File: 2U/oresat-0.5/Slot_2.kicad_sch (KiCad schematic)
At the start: 3 parts

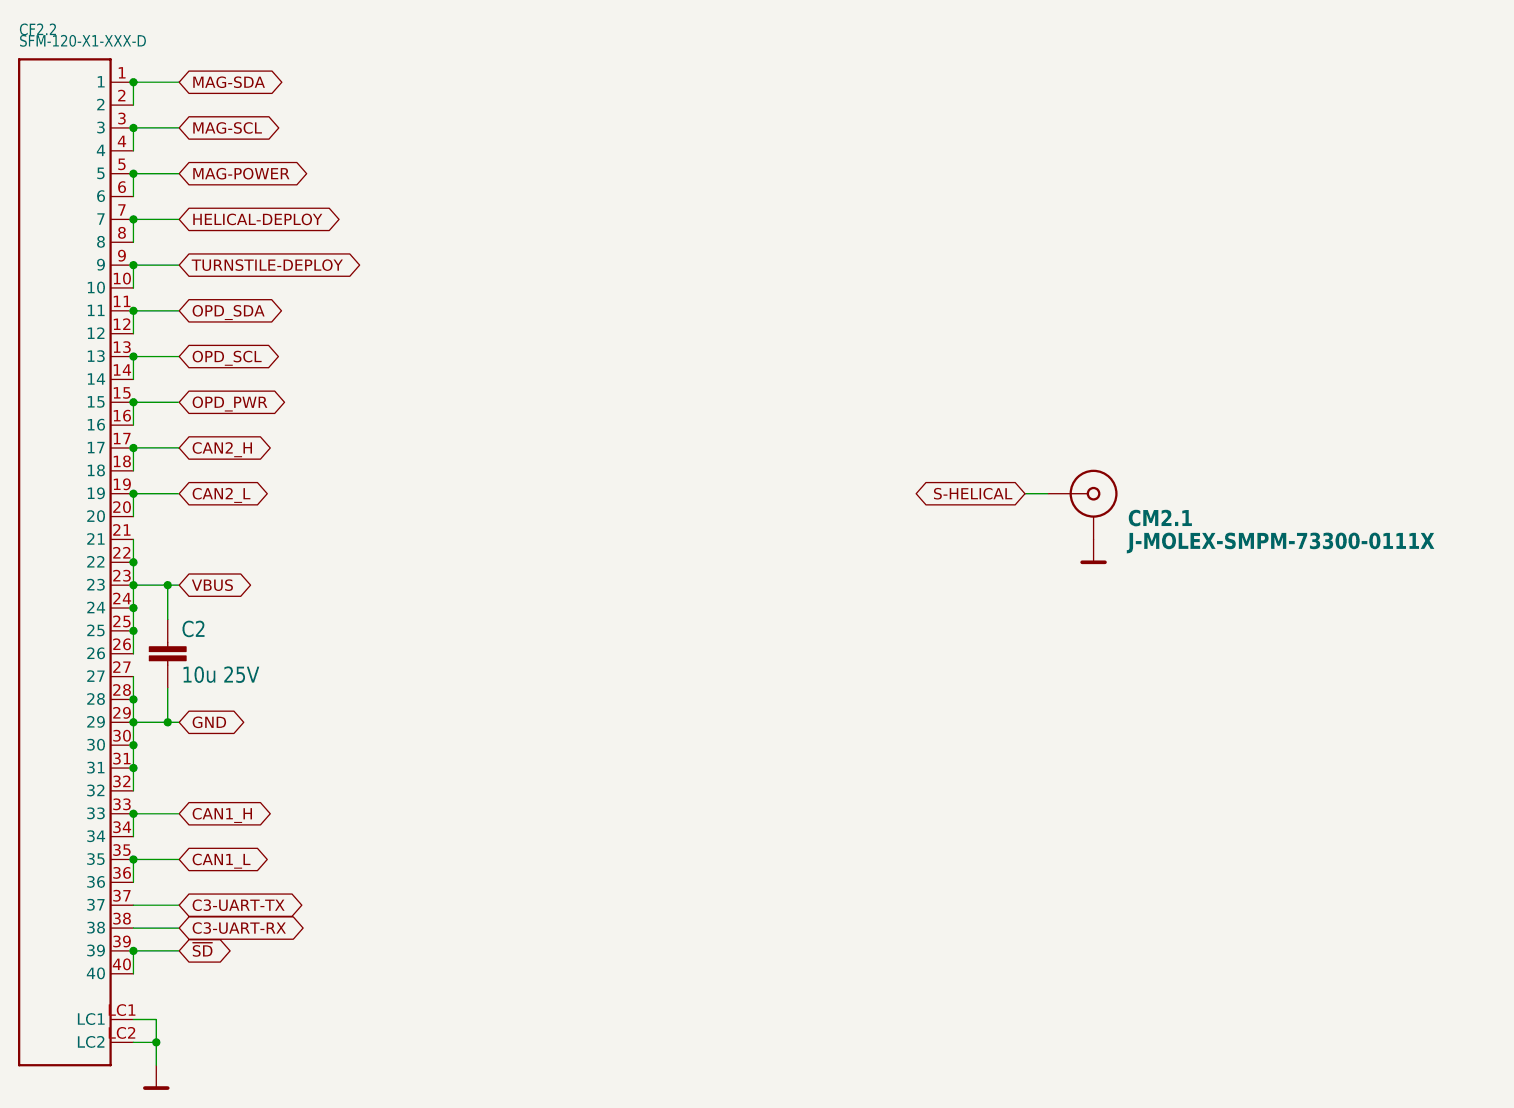
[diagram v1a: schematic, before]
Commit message: Fixed all (most) of the issues from Eagle imports
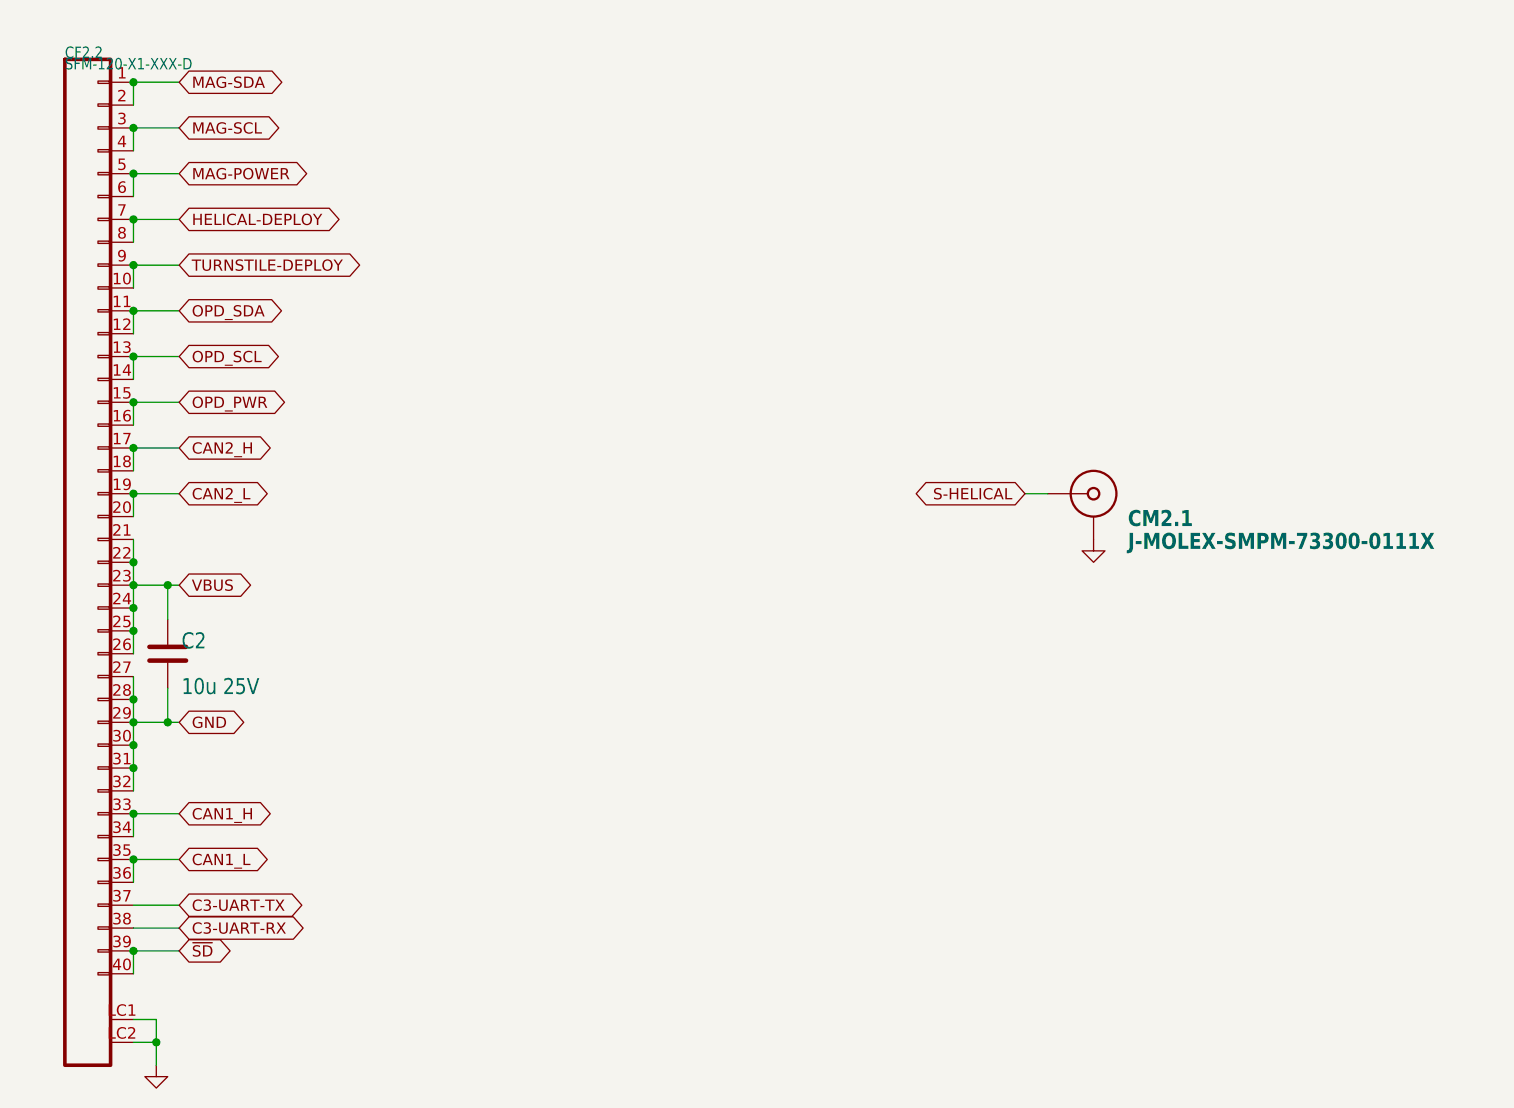
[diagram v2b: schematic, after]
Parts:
- C2: symbol oresat0-1u-backplane-eagle-import:C-EU1206-B -> Device:C
- CF2.2: symbol oresat-backplane-2u-eagle-import:SFM-120-X1-XXX-D -> oresat-connectors:J-SAMTEC-TFM-120-01-L-D-RA
- CM2.1: symbol oresat-symbols:J-MOLEX-SMPM-73300-0111X_1 -> oresat-connectors:J-MOLEX-SMPM-73300-0111X_1

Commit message: Moved entire schematic to single page
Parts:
- removed C2: 10u 25V, Capacitor_SMD:C_1206_3216Metric, symbol Device:C
- removed CF2.2: SFM-120-X1-XXX-D, oresat-connectors:J-SAMTEC-SFM-120-X1-XXX-D, symbol oresat-connectors:J-SAMTEC-TFM-120-01-L-D-RA
- removed CM2.1: J-MOLEX-SMPM-73300-0111X, oresat-connectors:J-MOLEX-SMPM-73300-0111X-long, symbol oresat-connectors:J-MOLEX-SMPM-73300-0111X_1
